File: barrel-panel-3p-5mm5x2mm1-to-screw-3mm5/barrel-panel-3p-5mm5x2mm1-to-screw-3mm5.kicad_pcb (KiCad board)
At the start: 2 copper layers, 9.8 x 22.4 mm, 2 parts, among them J1 Barrel_Jack_Switch, J2 Conn_01x02_Male

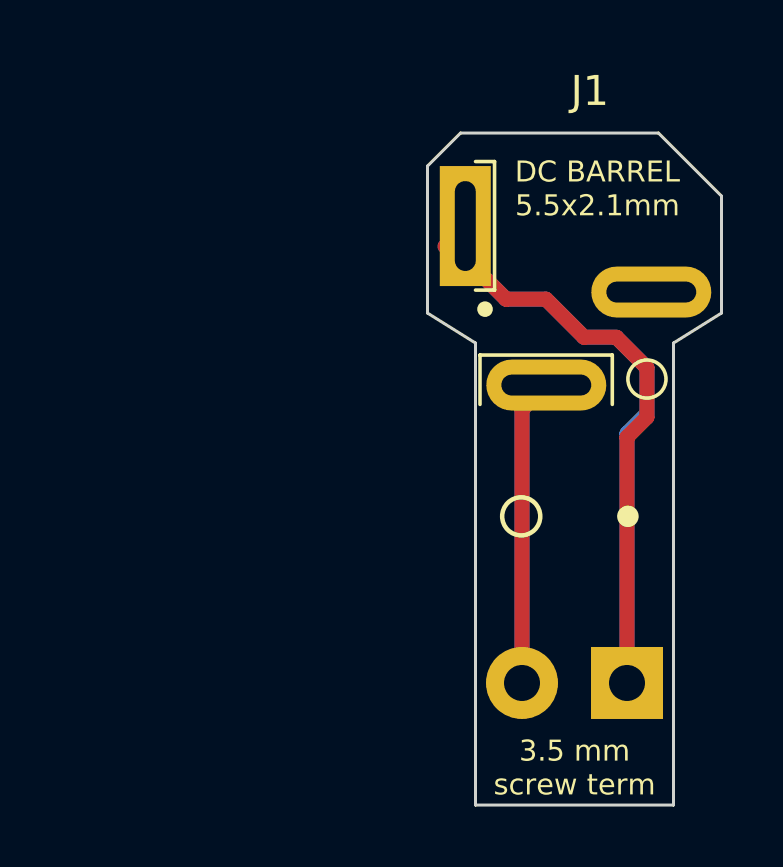
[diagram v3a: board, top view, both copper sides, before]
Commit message: fixed board to ease nut insertion
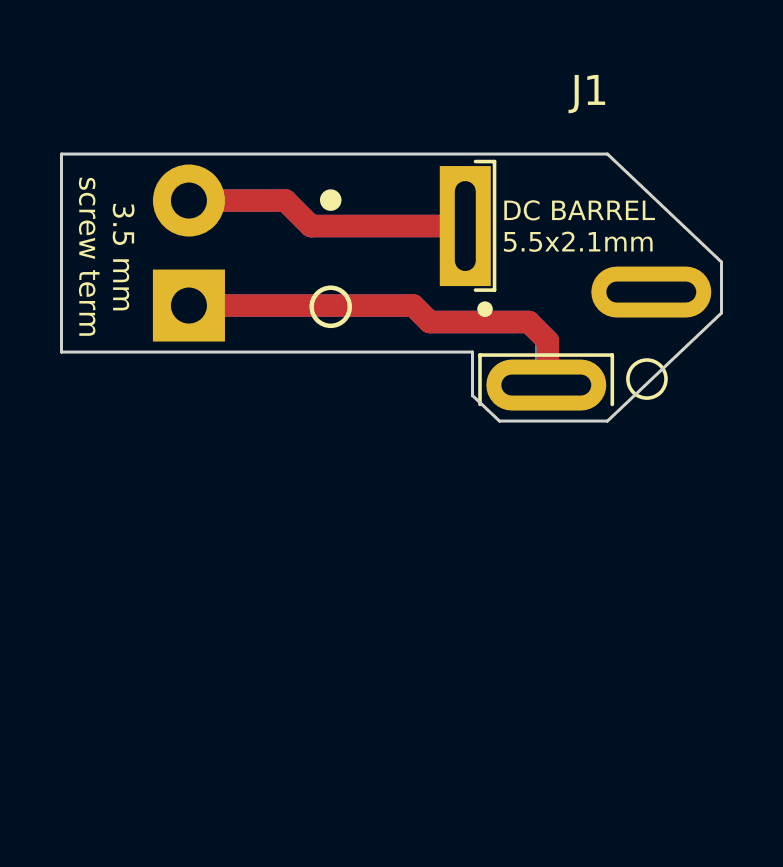
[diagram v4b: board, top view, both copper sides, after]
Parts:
- moved J2 19.3 mm to (92.0, 105.8), turned to 90 degrees
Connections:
- J2 pad 1: Net-(J1-Pad1) -> Net-(J1-Pad2)
- J2 pad 2: Net-(J1-Pad2) -> Net-(J1-Pad1)
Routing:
- net Net-(J1-Pad1): track 40.8 -> 19.1 mm
- net Net-(J1-Pad2): track 20.6 -> 27.8 mm
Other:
- board size 9.8 x 22.4 mm -> 22 x 8.9 mm
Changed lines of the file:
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@@
   )
   (footprint "TerminalBlock_4Ucon:TerminalBlock_4Ucon_1x02_P3.50mm_Horizontal" (layer "B.Cu")
-    (at 106.65 118.331 180)
+    (at 92.048 105.75 90)
     (descr "Terminal Block 4Ucon ItemNo. 19963, 2 pins, pitch 3.5mm, size 7.7x7mm^2, drill diamater 1.2mm, pad diameter 2.4mm, see http://www.4uconnector.com/online/object/4udrawing/19963.pdf, script-generated using https://github.com/pointhi/kicad-footprint-generator/scripts/TerminalBlock_4Ucon")
     (tags "THT Terminal Block 4Ucon ItemNo. 19963 pitch 3.5mm size 7.7x7mm^2 drill 1.2mm pad 2.4mm")
@@
     (property "Sheetname" "")
     (attr through_hole)
-    (fp_text reference "J2" (at 1.748 4.92) (layer "B.SilkS")
+    (fp_text reference "J2" (at 1.748 4.92 90) (layer "B.SilkS")
       (effects (font (size 1 1) (thickness 0.15)) (justify mirror))
     )
-    (fp_text value "Conn_01x02_Male" (at 1.75 -4.66) (layer "B.Fab")
+    (fp_text value "Conn_01x02_Male" (at 1.75 -4.66 90) (layer "B.Fab")
       (effects (font (size 1 1) (thickness 0.15)) (justify mirror))
     )
-    (fp_text user "${REFERENCE}" (at 1.75 -2.9) (layer "B.Fab")
+    (fp_text user "${REFERENCE}" (at 1.75 -2.9 90) (layer "B.Fab")
       (effects (font (size 1 1) (thickness 0.15)) (justify mirror))
     )
@@
     (fp_circle (center 0 0) (end 1.375 0) (layer "B.Fab") (width 0.1) (fill none))
     (fp_circle (center 3.5 0) (end 4.875 0) (layer "B.Fab") (width 0.1) (fill none))
-    (pad "1" thru_hole rect (at 0 0 180) (size 2.4 2.4) (drill 1.2) (layers *.Cu *.Mask)
-      (net 1 "Net-(J1-Pad1)") (pinfunction "Pin_1") (pintype "passive"))
-    (pad "2" thru_hole circle (at 3.5 0 180) (size 2.4 2.4) (drill 1.2) (layers *.Cu *.Mask)
-      (net 2 "Net-(J1-Pad2)") (pinfunction "Pin_2") (pintype "passive"))
+    (pad "1" thru_hole rect (at 0 0 90) (size 2.4 2.4) (drill 1.2) (layers *.Cu *.Mask)
+      (net 2 "Net-(J1-Pad2)") (pinfunction "Pin_1") (pintype "passive"))
+    (pad "2" thru_hole circle (at 3.5 0 90) (size 2.4 2.4) (drill 1.2) (layers *.Cu *.Mask)
+      (net 1 "Net-(J1-Pad1)") (pinfunction "Pin_2") (pintype "passive"))
     (model "${KICAD6_3DMODEL_DIR}/TerminalBlock_4Ucon.3dshapes/TerminalBlock_4Ucon_1x02_P3.50mm_Horizontal.wrl"
       (offset (xyz 0 0 0))
@@
     )
   )
-  (gr_circle (center 106.68 113.411) (end 106.963981 113.411) (layer "B.SilkS") (width 0.15) (fill solid))
-  (gr_circle (center 103.124 113.411) (end 103.759 113.411) (layer "B.SilkS") (width 0.15) (fill none))
-  (gr_circle (center 103.124 112.776) (end 103.632 112.395) (layer "F.SilkS") (width 0.15) (fill none))
-  (gr_circle (center 106.68 112.776) (end 106.963981 112.776) (layer "F.SilkS") (width 0.15) (fill solid))
-  (gr_line (start 101.1 100) (end 107.7 100) (layer "Edge.Cuts") (width 0.1))
-  (gr_line (start 108.2 107) (end 109.8 106) (layer "Edge.Cuts") (width 0.1))
-  (gr_line (start 100 101.1) (end 100 106) (layer "Edge.Cuts") (width 0.1))
-  (gr_line (start 101.6 122.4) (end 108.2 122.4) (layer "Edge.Cuts") (width 0.1))
-  (gr_line (start 100 106) (end 101.6 107) (layer "Edge.Cuts") (width 0.1))
-  (gr_line (start 107.7 100) (end 109.8 102.1) (layer "Edge.Cuts") (width 0.1))
-  (gr_line (start 101.1 100) (end 100 101.1) (layer "Edge.Cuts") (width 0.1))
-  (gr_line (start 109.8 102.1) (end 109.8 106) (layer "Edge.Cuts") (width 0.1))
-  (gr_line (start 108.2 107) (end 108.2 122.4) (layer "Edge.Cuts") (width 0.1))
-  (gr_line (start 101.6 107) (end 101.6 122.4) (layer "Edge.Cuts") (width 0.1))
-  (gr_text "DC BARREL\n5.5x2.1mm" (at 105.537 102.87) (layer "B.SilkS")
-    (effects (font (size 0.7 0.7) (thickness 0.175)) (justify mirror))
+  (gr_circle (center 97.409001 102.235) (end 97.409 101.95102) (layer "B.SilkS") (width 0.15) (fill solid))
+  (gr_circle (center 97.409 105.791) (end 97.409001 105.156) (layer "B.SilkS") (width 0.15) (fill none))
+  (gr_circle (center 96.774001 105.791001) (end 96.393001 105.283) (layer "F.SilkS") (width 0.15) (fill none))
+  (gr_circle (center 96.774001 102.235) (end 96.774001 101.951019) (layer "F.SilkS") (width 0.15) (fill solid))
+  (gr_line (start 87.8 100.7) (end 106 100.7) (layer "Edge.Cuts") (width 0.1))
+  (gr_line (start 106 109.6) (end 109.8 106) (layer "Edge.Cuts") (width 0.1))
+  (gr_line (start 87.8 100.7) (end 87.8 107.3) (layer "Edge.Cuts") (width 0.1))
+  (gr_line (start 101.5 107.3) (end 101.5 108.75) (layer "Edge.Cuts") (width 0.1))
+  (gr_line (start 102.4 109.6) (end 106 109.6) (layer "Edge.Cuts") (width 0.1))
+  (gr_line (start 106 100.7) (end 109.8 104.3) (layer "Edge.Cuts") (width 0.1))
+  (gr_line (start 101.5 108.75) (end 102.4 109.6) (layer "Edge.Cuts") (width 0.1))
+  (gr_line (start 109.8 104.3) (end 109.8 106) (layer "Edge.Cuts") (width 0.1))
+  (gr_line (start 87.8 107.3) (end 101.5 107.3) (layer "Edge.Cuts") (width 0.1))
+  (gr_text "DC BARREL\n5.5x2.1mm" (at 105.029 103.251) (layer "B.SilkS")
+    (effects (font (size 0.65 0.65) (thickness 0.1625)) (justify mirror))
   )
-  (gr_text "DC BARREL\n5.5x2.1mm" (at 105.664 101.854) (layer "F.SilkS")
+  (gr_text "DC BARREL\n5.5x2.1mm" (at 105.029 103.124) (layer "F.SilkS")
+    (effects (font (size 0.65 0.65) (thickness 0.1625)))
+  )
+  (gr_text "3.5 mm\nscrew term" (at 89.281 104.14 -90) (layer "F.SilkS")
     (effects (font (size 0.7 0.7) (thickness 0.175)))
   )
-  (gr_text "3.5 mm\nscrew term" (at 104.902 121.158) (layer "F.SilkS")
-    (effects (font (size 0.7 0.7) (thickness 0.175)))
-  )
-  (segment (start 102.616 105.537) (end 103.9495 105.537) (width 0.5) (layer "F.Cu") (net 1))
-  (segment (start 101.26 104.181) (end 102.616 105.537) (width 0.5) (layer "F.Cu") (net 1))
-  (segment (start 106.65 110.139) (end 106.65 118.331) (width 0.5) (layer "F.Cu") (net 1))
-  (segment (start 101.26 103.1) (end 101.26 104.181) (width 0.5) (layer "F.Cu") (net 1))
-  (segment (start 103.9495 105.537) (end 105.2195 106.807) (width 0.5) (layer "F.Cu") (net 1))
-  (segment (start 101.26 103.1) (end 100.584 103.776) (width 0.5) (layer "F.Cu") (net 1))
-  (segment (start 107.315 107.823) (end 107.315 109.474) (width 0.5) (layer "F.Cu") (net 1))
-  (segment (start 107.315 109.474) (end 106.65 110.139) (width 0.5) (layer "F.Cu") (net 1))
-  (segment (start 106.299 106.807) (end 107.315 107.823) (width 0.5) (layer "F.Cu") (net 1))
-  (segment (start 105.2195 106.807) (end 106.299 106.807) (width 0.5) (layer "F.Cu") (net 1))
-  (segment (start 106.65 118.331) (end 106.65 110.012) (width 0.5) (layer "B.Cu") (net 1))
-  (segment (start 101.26 104.181) (end 101.26 103.1) (width 0.5) (layer "B.Cu") (net 1))
-  (segment (start 105.2195 106.807) (end 103.9495 105.537) (width 0.5) (layer "B.Cu") (net 1))
-  (segment (start 103.9495 105.537) (end 102.616 105.537) (width 0.5) (layer "B.Cu") (net 1))
-  (segment (start 106.65 110.012) (end 107.315 109.347) (width 0.5) (layer "B.Cu") (net 1))
-  (segment (start 106.299 106.807) (end 105.2195 106.807) (width 0.5) (layer "B.Cu") (net 1))
-  (segment (start 107.315 109.347) (end 107.315 107.823) (width 0.5) (layer "B.Cu") (net 1))
-  (segment (start 102.616 105.537) (end 101.26 104.181) (width 0.5) (layer "B.Cu") (net 1))
-  (segment (start 107.315 107.823) (end 106.299 106.807) (width 0.5) (layer "B.Cu") (net 1))
-  (segment (start 101.26 103.1) (end 100.584 103.776) (width 0.5) (layer "B.Cu") (net 1))
-  (segment (start 103.15 109.21) (end 103.96 108.4) (width 0.5) (layer "F.Cu") (net 2))
-  (segment (start 103.15 118.331) (end 103.15 109.21) (width 0.5) (layer "F.Cu") (net 2))
-  (segment (start 103.15 109.21) (end 103.96 108.4) (width 0.5) (layer "B.Cu") (net 2))
-  (segment (start 103.124 118.305) (end 103.15 118.331) (width 0.5) (layer "B.Cu") (net 2))
-  (segment (start 103.15 118.331) (end 103.15 109.21) (width 0.5) (layer "B.Cu") (net 2))
+  (segment (start 96.115 103.1) (end 101.26 103.1) (width 0.75) (layer "F.Cu") (net 1))
+  (segment (start 92.048 102.25) (end 95.265 102.25) (width 0.75) (layer "F.Cu") (net 1))
+  (segment (start 95.265 102.25) (end 96.115 103.1) (width 0.75) (layer "F.Cu") (net 1))
+  (segment (start 95.265 102.25) (end 92.048 102.25) (width 0.75) (layer "B.Cu") (net 1))
+  (segment (start 101.26 103.1) (end 96.115 103.1) (width 0.75) (layer "B.Cu") (net 1))
+  (segment (start 96.115 103.1) (end 95.265 102.25) (width 0.75) (layer "B.Cu") (net 1))
+  (segment (start 100.076 106.299) (end 103.378 106.299) (width 0.75) (layer "F.Cu") (net 2))
+  (segment (start 103.378 106.299) (end 104.013 106.934) (width 0.75) (layer "F.Cu") (net 2))
+  (segment (start 104.013 106.934) (end 104.013 108.347) (width 0.75) (layer "F.Cu") (net 2))
+  (segment (start 92.048 105.75) (end 99.527 105.75) (width 0.75) (layer "F.Cu") (net 2))
+  (segment (start 104.013 108.347) (end 103.96 108.4) (width 0.75) (layer "F.Cu") (net 2))
+  (segment (start 99.527 105.75) (end 100.076 106.299) (width 0.75) (layer "F.Cu") (net 2))
+  (segment (start 103.96 106.881) (end 103.96 108.4) (width 0.75) (layer "B.Cu") (net 2))
+  (segment (start 103.378 106.299) (end 103.96 106.881) (width 0.75) (layer "B.Cu") (net 2))
+  (segment (start 92.048 105.75) (end 99.527 105.75) (width 0.75) (layer "B.Cu") (net 2))
+  (segment (start 99.527 105.75) (end 100.076 106.299) (width 0.75) (layer "B.Cu") (net 2))
+  (segment (start 100.076 106.299) (end 103.378 106.299) (width 0.75) (layer "B.Cu") (net 2))
 )
